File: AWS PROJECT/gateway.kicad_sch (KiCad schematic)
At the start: 151 parts, among them J1 10118194-0001LF, J10 SIM7100-8-1-15-00-A_REVC, J11 Conn_01x02_Pin, J12 Conn_01x02_Pin, J13 Conn_01x02_Pin, J14 B2B-XH-A_LF__SN_, J15 B2B-XH-A_LF__SN_, J16 B4B-XH-A_LF__SN_, J17 B4B-XH-A_LF__SN_, J18 B4B-XH-A_LF__SN_, J19 MEM2067-02-180-00-A_REVB, J2 Conn_01x02_Pin, J20 B3B-XH-A_LF__SN_, J21 B3B-XH-A_LF__SN_, J23 B4B-XH-A_LF__SN_, J24 B2B-XH-A_LF__SN_, J28 B4B-XH-A_LF__SN_, J29 B2B-XH-A_LF__SN_, J3 Conn_01x01_Pin, J31 TYPE-C-31-M-12, J32 B3B-XH-A_LF__SN_, J37 B3B-XH-A_LF__SN_, J4 Conn_01x01_Pin, J5 Conn_01x01_Pin, J6 Conn_01x01_Pin, J7 Conn_01x01_Pin, J8 Conn_01x01_Pin, J9 Conn_01x04_Pin, Q1 MMBT3904, Q2 MMBT3904, Q3 MMBT3904, SW1 SW_SPST, SW2 SW_SPST, SW3 SW_SPST, SW4 SW_SPST, U1 TXB0108RGYR, U14 AMS1117-3.3, U2 ESP32-WROOM-32E__4MB_HIGH_TEM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, U3 SIM7000E, U4 MPL3115A2, U6 DS3231MZ_TRL, U7 Ai-Thinker RA-08H, U8 ST3485EBDR, U9 FT232RL-REEL

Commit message: updates to the code and hardware, testing complete
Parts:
- removed R31, R32: 4.7k, Resistor_SMD:R_0603_1608Metric, symbol Device:R
- removed R33: 10k, Resistor_SMD:R_0603_1608Metric, symbol Device:R
- removed SW4: SW_SPST, Button_Switch_THT:SW_PUSH_6mm, symbol Switch:SW_SPST
- added J34: Conn_01x01_Pin, Connector_PinHeader_1.00mm:PinHeader_1x01_P1.00mm_Vertical, symbol Connector:Conn_01x01_Pin
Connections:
- net -rs485 en: now also U8.3 (DE)
- net 32khz: no longer U2.4 (SENSOR_VP)
- net DAVIS 7852: now also U2.6 (IO34); no longer U2.8 (IO32)
- net I2C SCL: no longer U7.14 (IO14)
- net I2C SDA: no longer U7.13 (IO15)
- net LORA RST: now also U2.8 (IO32)
- net SD CS: now also U2.26 (IO4); no longer U2.13 (IO14)
- net gsm power key: now also U2.13 (IO14); no longer U2.26 (IO4)
- net gsm reset: now also J34.1 (Pin_1); no longer U2.5 (SENSOR_VN)
- net at J13.2 (Pin_2): now also U7.13 (IO15); no longer U7.10 (LPRXD/IO60)
- net ESP_RX: now reaches U7.11 (TXD/IO17)
- net ESP_RX: now also J12.2 (Pin_2), U1.20 (B1), U2.27 (IO16); no longer J12.1 (Pin_1)
- net at U7.12 (RXD/IO16): now also J13.1 (Pin_1); no longer J12.2 (Pin_2)
- net RX renamed ESP_TX
- net ESP_TX: now also J12.1 (Pin_1), U2.28 (IO17), U7.10 (LPRXD/IO60); no longer U2.27 (IO16)
- removed net TX: U1.20 (B1), U2.28 (IO17)
- removed net rs485 en: U2.6 (IO34), U8.3 (DE)
- no-connect marks 50 -> 49
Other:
- note added: "PROPER UART CONNECTION"
- note added: "RESET CONTROLLED BY ESP32"
- note removed: "reset shcematic refernced from resources"
- moved on the sheet: J12, J13, J7

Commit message: updates to gateway board
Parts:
- removed D10: PESDHC2FD4V5B, Package_DFN_QFN:Diodes_DFN1006-3, symbol diode:Diode
- removed FB2: FerriteBead_Small, BLM03HG601SZ1D:BEADC0603X33N, symbol Device:FerriteBead_Small
- removed J1: 10118194-0001LF, 10118194-0001LF:AMPHENOL_10118194-0001LF, symbol 10118194-0001LF:10118194-0001LF
- removed J11: Conn_01x02_Pin, Connector_PinHeader_1.00mm:PinHeader_1x02_P1.00mm_Vertical, symbol Connector:Conn_01x02_Pin
- removed J3, J34, J4, J5, J6, J7, J8: Conn_01x01_Pin, Connector_PinHeader_1.00mm:PinHeader_1x01_P1.00mm_Vertical, symbol Connector:Conn_01x01_Pin
- removed SW1, SW2, SW3: SW_SPST, Button_Switch_THT:SW_PUSH_6mm, symbol Switch:SW_SPST
- added J1, J35, J38, J39: Conn_01x02_Pin, Connector_PinHeader_2.54mm:PinHeader_1x02_P2.54mm_Vertical, symbol Connector:Conn_01x02_Pin
- added J40: Conn_01x06_Pin, Connector_PinHeader_2.54mm:PinHeader_1x06_P2.54mm_Vertical, symbol Connector:Conn_01x06_Pin
- added SNS_TX10, SNS_TX11, SNS_TX12, SNS_TX13, SNS_TX14, SNS_TX7, SNS_TX8, SNS_TX9: TestPoint, TestPoint:TestPoint_Pad_D1.5mm, symbol Connector:TestPoint
- J12, J13, J2: footprint Connector_PinHeader_1.00mm:PinHeader_1x02_P1.00mm_Vertical -> Connector_PinHeader_2.54mm:PinHeader_1x02_P2.54mm_Vertical
- J9: footprint Connector_PinHeader_1.00mm:PinHeader_1x04_P1.00mm_Vertical -> Connector_PinHeader_2.54mm:PinHeader_1x04_P2.54mm_Vertical
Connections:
- net strap 5 is gone; now on net strap12: J23.1
- net 32khz: now also SNS_TX8.1
- net D+: now also J1.1 (Pin_1)
- net D-: now also J1.2 (Pin_2)
- net DAVIS 7852: now also J40.1 (Pin_1)
- net DS18B20: now also J40.3 (Pin_3)
- net GND: now also J35.2 (Pin_2), J38.1 (Pin_1)
- net INSPEED VORTEX: now also J40.5 (Pin_5)
- net INSPEEED VANE: now also J40.6 (Pin_6)
- net LORA BOOT: now also J39.2 (Pin_2)
- net RTC INT: now also SNS_TX9.1
- net RTC RST: now also SNS_TX10.1
- net S1223: now also J40.2 (Pin_2)
- net VBUS: now also C38.1, C39.1, JP16.1 (A), U9.20 (VCC), U9.4 (VCCIO); no longer U3.24 (USB_VBUS)
- net VH400: now also J40.4 (Pin_4)
- net gsm reset: now also SNS_TX13.1
- net lora power in: now also J39.1 (Pin_1)
- net at C4.2, C6.1, R6.2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: now also J35.1 (Pin_1)
- net at U7.14 (IO14): now also SNS_TX7.1
- net at U7.7 (SWC/IO7): now also SNS_TX11.1
- net at U7.8 (SWD/IO6): now also SNS_TX12.1
- net at U2.25 (IO0): now also J38.2 (Pin_2)
- new net: SNS_TX14.1, U3.24 (USB_VBUS)
- no-connect marks 49 -> 48

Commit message: updates to the power board
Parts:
- removed J23: B4B-XH-A_LF__SN_, B4B-XH-A_LF__SN_:JST_B4B-XH-A_LF__SN_, symbol B4B-XH-A_LF__SN_:B4B-XH-A_LF__SN_
- added C47, C51, C76: 10uF, Capacitor_SMD:C_0603_1608Metric, symbol Device:C_Small
- added C49, C67, C78: 1uF, Capacitor_SMD:C_0603_1608Metric, symbol Device:C_Small
- added D20, D21, D24, D25: 1N5819WS, Diode_SMD:D_SOD-323, symbol Diode:1N5819WS
- added JP10, JP15, JP22, JP23, JP24, JP25: Jumper_2_Small_Open, Jumper:SolderJumper-2_P1.3mm_Open_RoundedPad1.0x1.5mm, symbol Jumper:Jumper_2_Small_Open
- added U11, U16, U18: AMS1117-3.3, Package_TO_SOT_SMD:SOT-223-3_TabPin2, symbol Regulator_Linear:AMS1117-3.3
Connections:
- net 3v3: no longer J17.1, J28.1, JP1.2 (B), JP17.2 (B), JP2.2 (B), JP4.2 (B), JP6.2 (B), JP7.2 (B), JP8.2 (B)
- net 5v: now also JP10.2 (B), JP22.2 (B), JP24.2 (B)
- net GND: now also C47.2, C49.2, C51.2, C67.2, C76.2, C78.2, U11.1 (GND), U16.1 (GND), U18.1 (GND)
- net VCC: now also D20.2 (A); no longer C41.1, U14.3 (VI)
- new net: C41.1, D20.1 (K), U14.3 (VI)
- new net: C51.1, D25.1 (K), U16.3 (VI)
- new net: C47.1, D24.1 (K), U11.3 (VI)
- new net: C78.1, JP25.1 (A), U18.2 (VO)
- new net: C67.1, JP23.1 (A), U16.2 (VO)
- new net: C76.1, D21.1 (K), U18.3 (VI)
- new net: D21.2 (A), JP24.1 (A)
- new net: D25.2 (A), JP22.1 (A)
- new net: D24.2 (A), JP10.1 (A)
- new net: C49.1, JP15.1 (A), U11.2 (VO)
- new net +3.3V_ESP: JP1.2 (B), JP15.2 (B), JP17.2 (B), JP7.2 (B)
- new net +3.3V_GSM: JP2.2 (B), JP25.2 (B)
- new net +3.3V_LORA: J17.1, J28.1, JP23.2 (B), JP4.2 (B), JP6.2 (B), JP8.2 (B)
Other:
- moved on the sheet: C10, C4, C6, C9, D3, J2, J35, J38, J40, J9, JP1, R10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

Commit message: updates to gateway board
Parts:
- added SNS_TX1, SNS_TX15: TestPoint, TestPoint:TestPoint_Pad_D1.5mm, symbol Connector:TestPoint
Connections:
- net ESP_RX: no longer J12.2 (Pin_2), U7.11 (TXD/IO17)
- net ESP_TX: no longer J12.1 (Pin_1), U7.10 (LPRXD/IO60)
- net gsm power key: now also SNS_TX1.1; no longer U2.13 (IO14)
- net strap12: now also SNS_TX15.1
- net strap15 renamed LORA_TX
- net LORA_TX: now also J12.1 (Pin_1), U7.10 (LPRXD/IO60)
- new net LORA_RX: J12.2 (Pin_2), U2.13 (IO14), U7.11 (TXD/IO17)

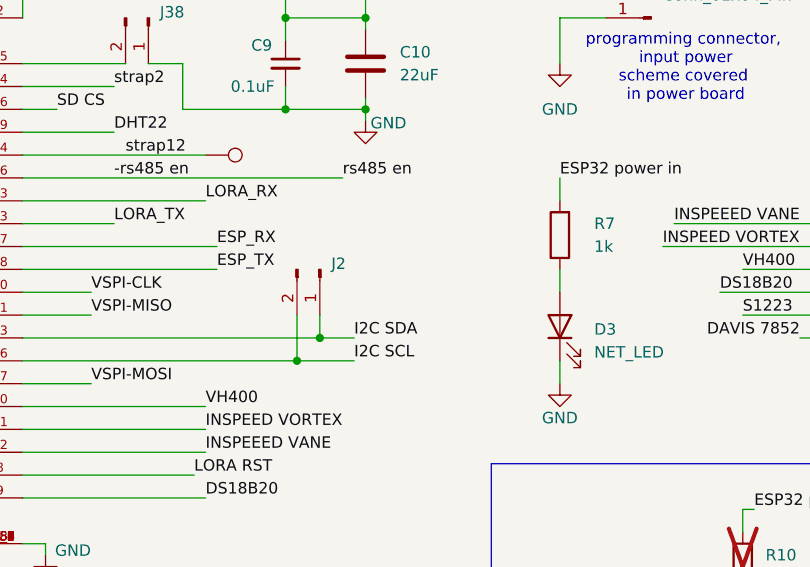
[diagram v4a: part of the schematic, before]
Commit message: fixed i2c error on pcb, added power monitoring code, tested all i2c slaves
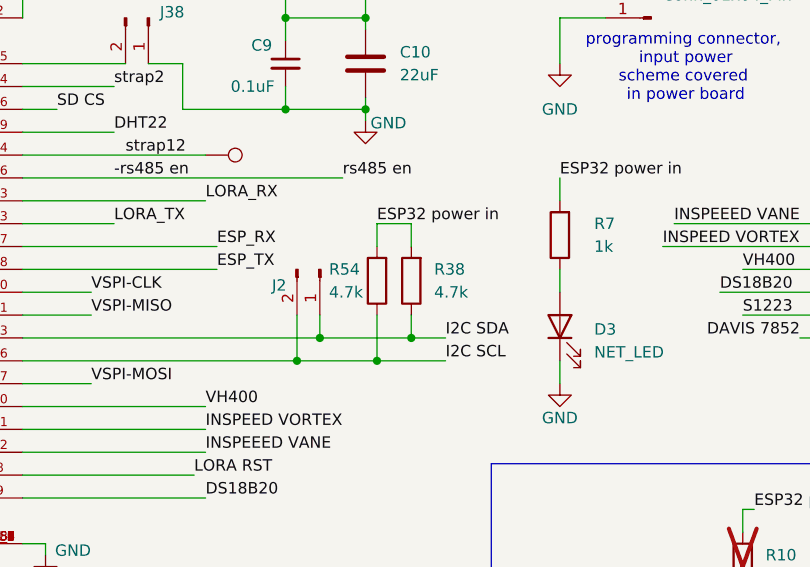
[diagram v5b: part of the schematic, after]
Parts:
- added R38, R54: 4.7k, Resistor_SMD:R_0603_1608Metric, symbol Device:R
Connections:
- net ESP32 power in: now also R38.2, R54.2
- net I2C SCL: now also R54.1
- net I2C SDA: now also R38.1
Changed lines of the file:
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@@
 	)
 	(junction
+		(at 168.91 391.16)
+		(diameter 0)
+		(color 0 0 0 0)
+	)
+	(junction
 		(at 496.57 220.98)
 		(diameter 0)
@@
 	)
 	(junction
+		(at 172.72 388.62)
+		(diameter 0)
+		(color 0 0 0 0)
+	)
+	(junction
 		(at 499.11 114.3)
 		(diameter 0)
@@
 	(wire
 		(pts
+			(xy 172.72 375.92) (xy 172.72 378.46)
+		)
+		(stroke
+			(width 0)
+			(type default)
+		)
+	)
+	(wire
+		(pts
 			(xy 102.87 190.5) (xy 118.11 190.5)
 		)
@@
 	(wire
 		(pts
+			(xy 168.91 386.08) (xy 168.91 391.16)
+		)
+		(stroke
+			(width 0)
+			(type default)
+		)
+	)
+	(wire
+		(pts
 			(xy 77.47 233.68) (xy 77.47 232.41)
 		)
@@
 	(wire
 		(pts
+			(xy 168.91 375.92) (xy 172.72 375.92)
+		)
+		(stroke
+			(width 0)
+			(type default)
+		)
+	)
+	(wire
+		(pts
 			(xy 621.03 218.44) (xy 618.49 218.44)
 		)
@@
 	(wire
 		(pts
-			(xy 162.56 388.62) (xy 166.37 388.62)
+			(xy 162.56 388.62) (xy 172.72 388.62)
 		)
 		(stroke
@@
 	(wire
 		(pts
-			(xy 160.02 391.16) (xy 166.37 391.16)
+			(xy 160.02 391.16) (xy 168.91 391.16)
 		)
 		(stroke
@@
 	(wire
 		(pts
+			(xy 168.91 378.46) (xy 168.91 375.92)
+		)
+		(stroke
+			(width 0)
+			(type default)
+		)
+	)
+	(wire
+		(pts
 			(xy 680.72 142.24) (xy 680.72 144.78)
 		)
@@
 	(wire
 		(pts
+			(xy 172.72 386.08) (xy 172.72 388.62)
+		)
+		(stroke
+			(width 0)
+			(type default)
+		)
+	)
+	(wire
+		(pts
 			(xy 725.17 214.63) (xy 760.73 214.63)
 		)
@@
 	(wire
 		(pts
+			(xy 168.91 391.16) (xy 176.53 391.16)
+		)
+		(stroke
+			(width 0)
+			(type default)
+		)
+	)
+	(wire
+		(pts
 			(xy 717.55 154.94) (xy 706.12 154.94)
 		)
@@
 	(wire
 		(pts
+			(xy 172.72 388.62) (xy 176.53 388.62)
+		)
+		(stroke
+			(width 0)
+			(type default)
+		)
+	)
+	(wire
+		(pts
 			(xy 162.56 386.08) (xy 162.56 388.62)
 		)
@@
 		)
 	)
+	(label "ESP32 power in"
+		(at 168.91 375.92 0)
+		(effects
+			(font
+				(size 1.27 1.27)
+			)
+			(justify left bottom)
+		)
+	)
 	(label "I2C SDA"
-		(at 166.37 388.62 0)
+		(at 176.53 388.62 0)
 		(effects
 			(font
@@
 	)
 	(label "I2C SCL"
-		(at 166.37 391.16 0)
+		(at 176.53 391.16 0)
 		(effects
 			(font
@@
 	)
 	(symbol
+		(lib_id "Device:R")
+		(at 168.91 382.27 180)
+		(unit 1)
+		(exclude_from_sim no)
+		(in_bom yes)
+		(on_board yes)
+		(dnp no)
+		(property "Reference" "R54"
+			(at 163.576 381 0)
+			(effects
+				(font
+					(size 1.27 1.27)
+				)
+				(justify right)
+			)
+		)
+		(property "Value" "4.7k"
+			(at 163.576 383.54 0)
+			(effects
+				(font
+					(size 1.27 1.27)
+				)
+				(justify right)
+			)
+		)
+		(property "Footprint" "Resistor_SMD:R_0603_1608Metric"
+			(at 170.688 382.27 90)
+			(effects
+				(font
+					(size 1.27 1.27)
+				)
+				(hide yes)
+			)
+		)
+		(property "Datasheet" "~"
+			(at 168.91 382.27 0)
+			(effects
+				(font
+					(size 1.27 1.27)
+				)
+				(hide yes)
+			)
+		)
+		(property "Description" "Resistor"
+			(at 168.91 382.27 0)
+			(effects
+				(font
+					(size 1.27 1.27)
+				)
+				(hide yes)
+			)
+		)
+		(pin "2"
+		)
+		(pin "1"
+		)
+		(instances
+			(project "AWS PROJECT"
+				(path "/28dd5718-f0db-4cd1-9b2d-c2f5533a75a3/918a84d0-2382-4e9e-a083-abfab5a808df"
+					(reference "R54")
+					(unit 1)
+				)
+			)
+		)
+	)
+	(symbol
 		(lib_id "Device:C_Small")
 		(at 464.82 430.53 0)
@@
 	)
 	(symbol
+		(lib_id "Device:R")
+		(at 172.72 382.27 180)
+		(unit 1)
+		(exclude_from_sim no)
+		(in_bom yes)
+		(on_board yes)
+		(dnp no)
+		(fields_autoplaced yes)
+		(property "Reference" "R38"
+			(at 175.26 380.9999 0)
+			(effects
+				(font
+					(size 1.27 1.27)
+				)
+				(justify right)
+			)
+		)
+		(property "Value" "4.7k"
+			(at 175.26 383.5399 0)
+			(effects
+				(font
+					(size 1.27 1.27)
+				)
+				(justify right)
+			)
+		)
+		(property "Footprint" "Resistor_SMD:R_0603_1608Metric"
+			(at 174.498 382.27 90)
+			(effects
+				(font
+					(size 1.27 1.27)
+				)
+				(hide yes)
+			)
+		)
+		(property "Datasheet" "~"
+			(at 172.72 382.27 0)
+			(effects
+				(font
+					(size 1.27 1.27)
+				)
+				(hide yes)
+			)
+		)
+		(property "Description" "Resistor"
+			(at 172.72 382.27 0)
+			(effects
+				(font
+					(size 1.27 1.27)
+				)
+				(hide yes)
+			)
+		)
+		(pin "2"
+		)
+		(pin "1"
+		)
+		(instances
+			(project "AWS PROJECT"
+				(path "/28dd5718-f0db-4cd1-9b2d-c2f5533a75a3/918a84d0-2382-4e9e-a083-abfab5a808df"
+					(reference "R38")
+					(unit 1)
+				)
+			)
+		)
+	)
+	(symbol
 		(lib_id "Connector:Conn_01x02_Pin")
 		(at 449.58 96.52 270)
@@
 		(on_board yes)
 		(dnp no)
-		(fields_autoplaced yes)
 		(property "Reference" "J2"
-			(at 163.83 380.3649 90)
+			(at 157.226 382.778 90)
 			(effects
 				(font

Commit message: updates to the gateway board
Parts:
- removed J16: B4B-XH-A_LF__SN_, B4B-XH-A_LF__SN_:JST_B4B-XH-A_LF__SN_, symbol B4B-XH-A_LF__SN_:B4B-XH-A_LF__SN_
- added J3: B3B-XH-A_LF__SN_, B3B-XH-A_LF__SN_:JST_B3B-XH-A_LF__SN_, symbol B3B-XH-A_LF__SN_:B3B-XH-A_LF__SN_
- added R55, R61: 4.7k, Resistor_SMD:R_0603_1608Metric, symbol Device:R
- added R62: 10K, Resistor_SMD:R_0603_1608Metric, symbol Device:R
- added R63: 20K, Resistor_SMD:R_0603_1608Metric, symbol Device:R
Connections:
- net 3v3: now also R55.2, R61.2
- net DAVIS 7852: now also J40.4 (Pin_4), U2.10 (IO25), J3.1, R61.1; no longer J40.1 (Pin_1), U2.6 (IO34)
- net GND: now also J3.2, J3.3, R63.1
- net INSPEED VORTEX: now also R55.1
- net INSPEEED VANE: now also R62.2, R63.2; no longer J37.2
- net VH400: now also J40.1 (Pin_1), U2.6 (IO34); no longer J40.4 (Pin_4), U2.10 (IO25)
- new net: J37.2, R62.1
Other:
- moved on the sheet: J14, J20
